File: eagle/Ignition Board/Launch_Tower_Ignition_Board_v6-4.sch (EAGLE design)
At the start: 43 parts, among them Q1 PMV45EN, U1 OPTOISOLATOR, U2 INVERT GATES, U3 SN65220DBV, U4 AND GATE

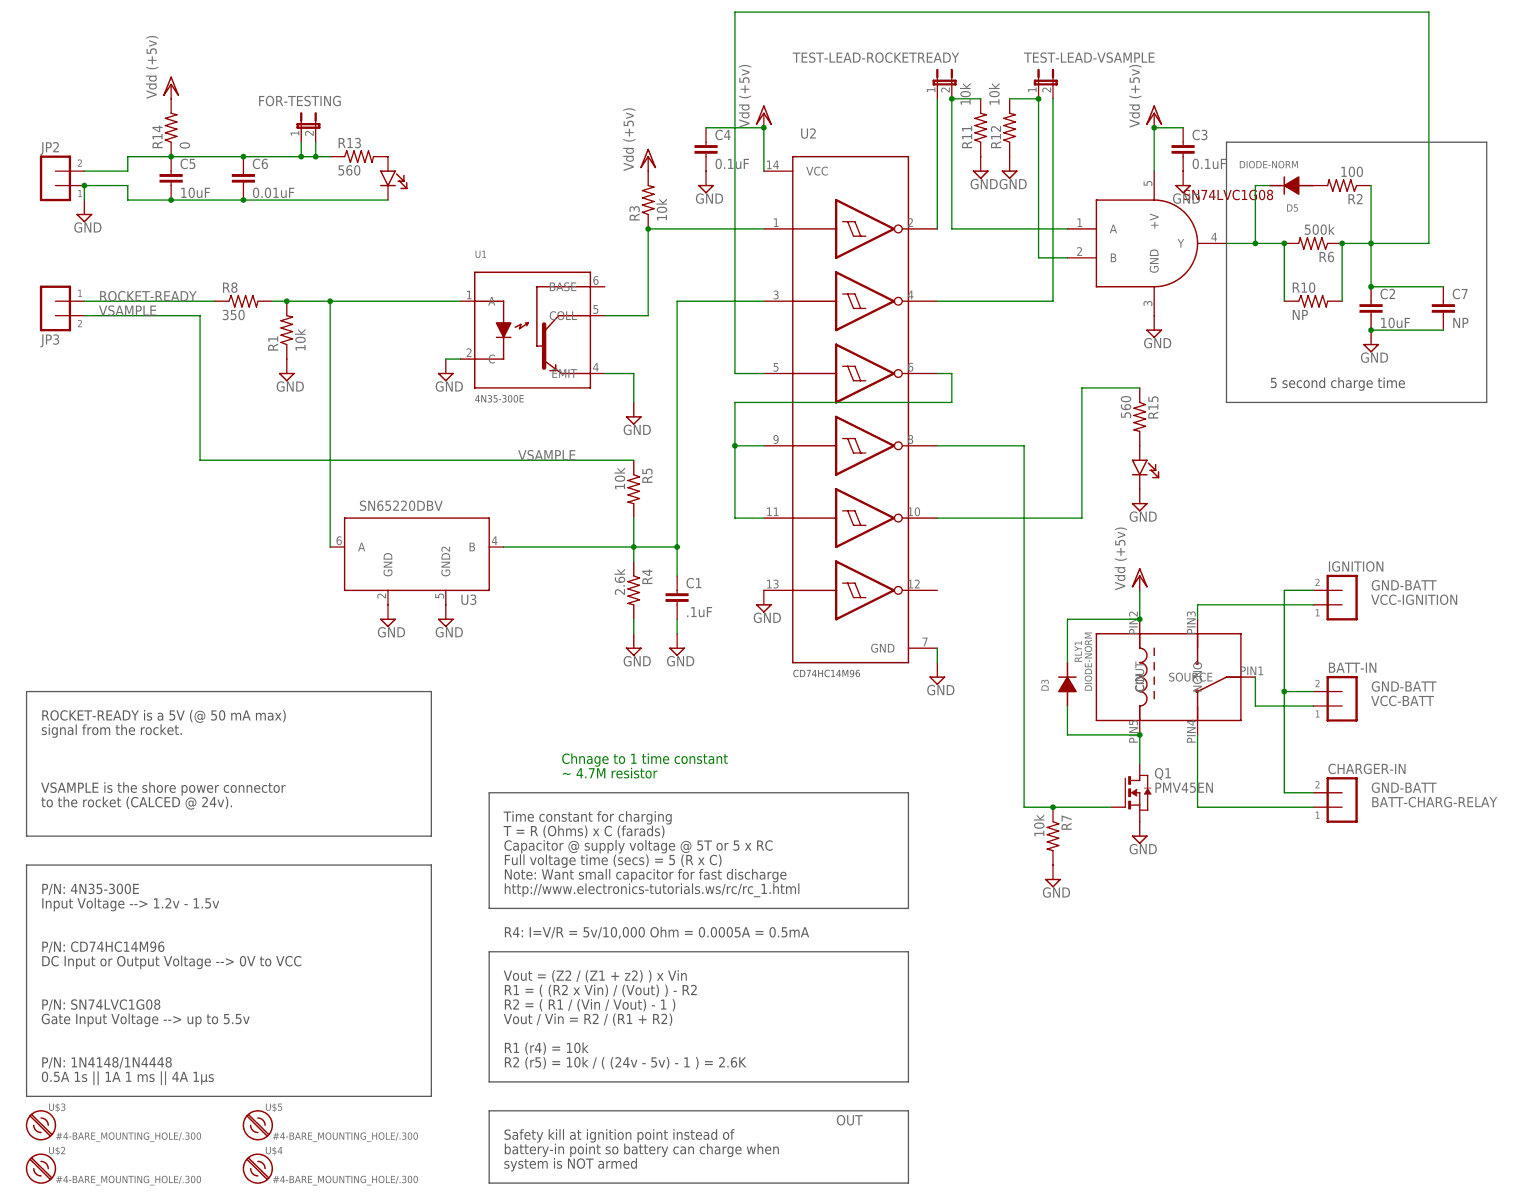
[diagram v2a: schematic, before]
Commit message: Updated Eagle File
Modified ignition board resistor R8
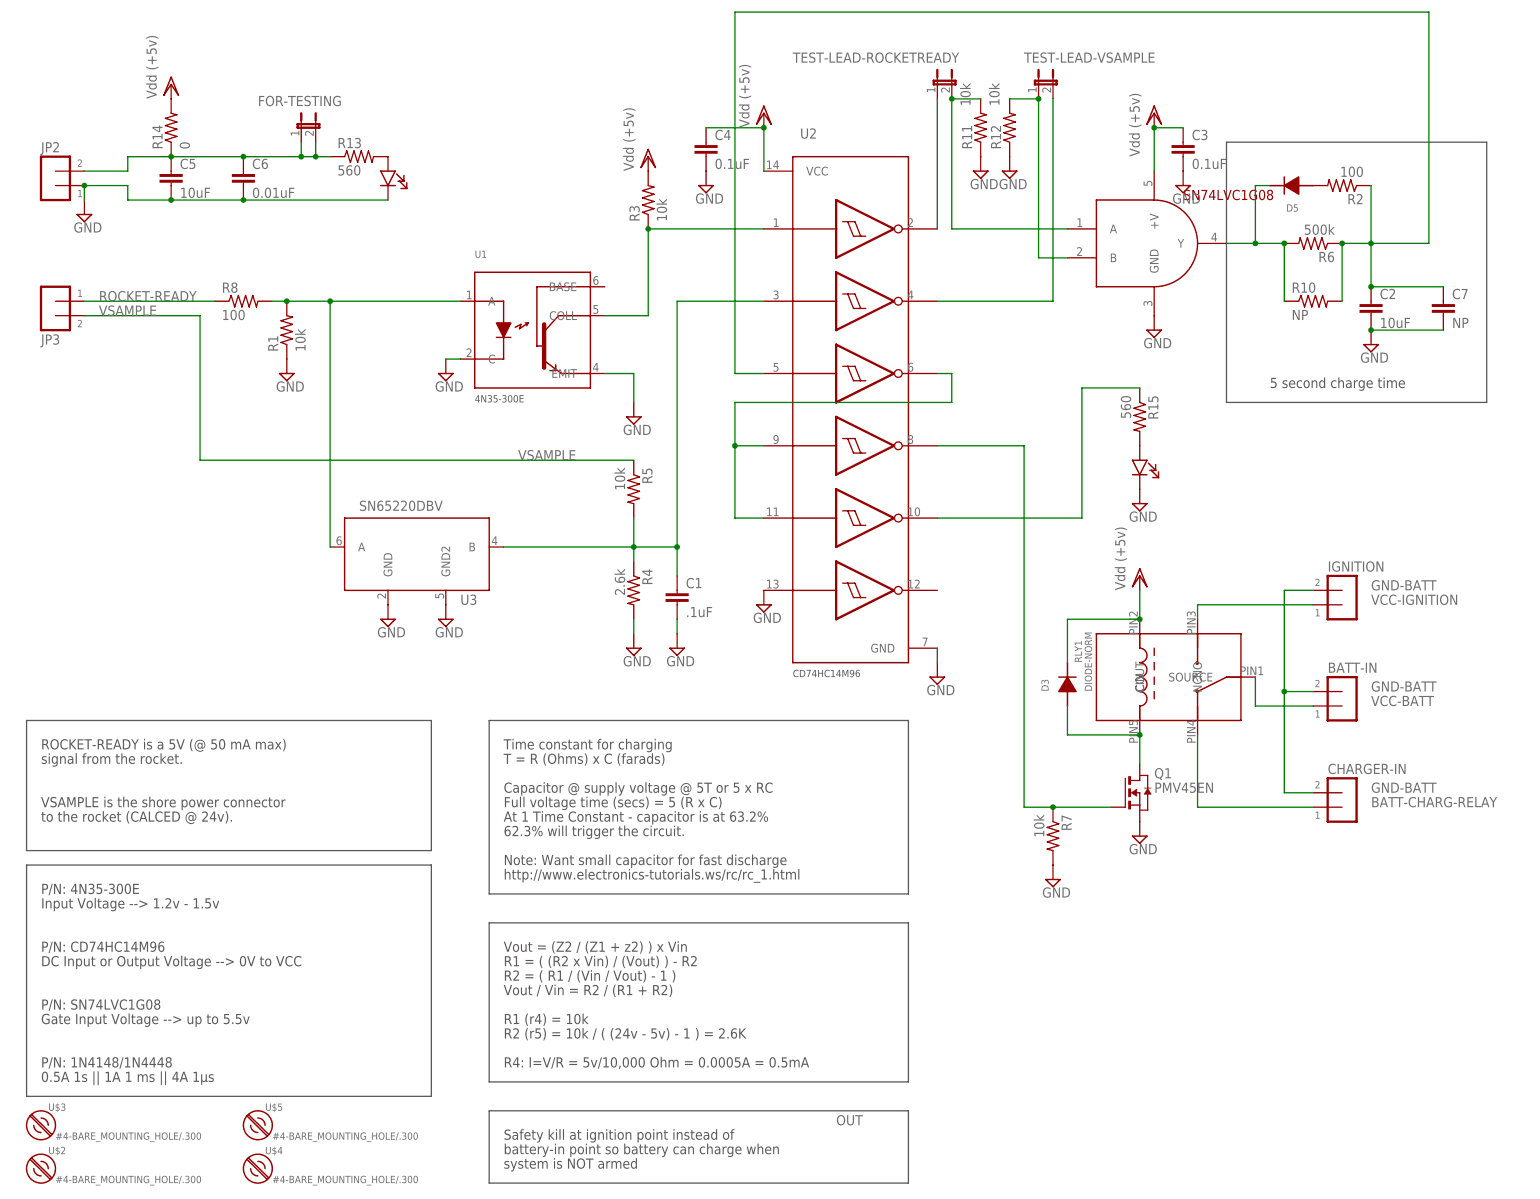
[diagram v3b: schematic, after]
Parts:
- R8: value 350 -> 100
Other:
- note added: "62.3% will trigger the circuit."
- note added: "At 1 Time Constant - capacitor is at 63.2%"
- note removed: "Chnage to 1 time constant"
- note removed: "~ 4.7M resistor"
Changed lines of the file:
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@@
 <?xml version="1.0" encoding="utf-8"?>
 <!DOCTYPE eagle SYSTEM "eagle.dtd">
-<eagle version="6.2">
+<eagle version="6.4">
 <drawing>
 <settings>
@@
 <part name="JP2" library="launch-tower" deviceset="SCREW-TERMINAL-5MM" device="" value=""/>
 <part name="JP3" library="launch-tower" deviceset="SCREW-TERMINAL-5MM" device="" value=""/>
-<part name="D5" library="launch-tower" deviceset="DIODE-NORM" device=""/>
+<part name="D5" library="launch-tower" deviceset="DIODE-NORM" device="" value=""/>
 <part name="D3" library="launch-tower" deviceset="DIODE-NORM" device=""/>
 <part name="VDD2" library="supply1" deviceset="VDD" device="" value="Vdd (+5v)"/>
@@
 <part name="TEST-LEAD-VSAMPLE" library="SparkFun" deviceset="JUMPER-2" device="PTH"/>
 <part name="LED-POWER-INDICATOR" library="launch-tower" deviceset="LED-550-XX04" device=""/>
-<part name="R8" library="rcl_custom" deviceset="R-US_" device="0805-B" value="350"/>
+<part name="R8" library="rcl_custom" deviceset="R-US_" device="0805-B" value="100"/>
 <part name="R1" library="rcl_custom" deviceset="R-US_" device="0805-B" value="10k"/>
 <part name="R3" library="rcl_custom" deviceset="R-US_" device="0805-B" value="10k"/>
@@
 <sheet>
 <plain>
-<text x="12.7" y="83.82" size="1.778" layer="97">ROCKET-READY is a 5V (@ 50 mA max)</text>
-<text x="12.7" y="81.28" size="1.778" layer="97">signal from the rocket.</text>
-<text x="12.7" y="71.12" size="1.778" layer="97">VSAMPLE is the shore power connector</text>
-<text x="12.7" y="68.58" size="1.778" layer="97">to the rocket (CALCED @ 24v).</text>
+<text x="12.7" y="78.74" size="1.778" layer="97">ROCKET-READY is a 5V (@ 50 mA max)</text>
+<text x="12.7" y="76.2" size="1.778" layer="97">signal from the rocket.</text>
+<text x="12.7" y="68.58" size="1.778" layer="97">VSAMPLE is the shore power connector</text>
+<text x="12.7" y="66.04" size="1.778" layer="97">to the rocket (CALCED @ 24v).</text>
 <text x="152.4" y="12.7" size="1.778" layer="104">OUT</text>
 <text x="152.4" y="12.7" size="1.778" layer="104">OUT</text>
 <text x="152.4" y="12.7" size="1.778" layer="95">OUT</text>
-<text x="93.98" y="45.72" size="1.778" layer="97">R4: I=V/R = 5v/10,000 Ohm = 0.0005A = 0.5mA</text>
-<text x="93.98" y="66.04" size="1.778" layer="97">Time constant for charging</text>
-<text x="93.98" y="63.5" size="1.778" layer="97">T = R (Ohms) x C (farads)</text>
-<text x="93.98" y="60.96" size="1.778" layer="97">Capacitor @ supply voltage @ 5T or 5 x RC</text>
-<text x="93.98" y="58.42" size="1.778" layer="97">Full voltage time (secs) = 5 (R x C)</text>
-<text x="93.98" y="55.88" size="1.778" layer="97">Note: Want small capacitor for fast discharge</text>
-<text x="93.98" y="38.1" size="1.778" layer="97">Vout = (Z2 / (Z1 + z2) ) x Vin</text>
-<text x="93.98" y="35.56" size="1.778" layer="97">R1 = ( (R2 x Vin) / (Vout) ) - R2</text>
-<text x="93.98" y="33.02" size="1.778" layer="97">R2 = ( R1 / (Vin / Vout) - 1 )</text>
-<text x="93.98" y="30.48" size="1.778" layer="97">Vout / Vin = R2 / (R1 + R2)</text>
+<text x="93.98" y="22.86" size="1.778" layer="97">R4: I=V/R = 5v/10,000 Ohm = 0.0005A = 0.5mA</text>
+<text x="93.98" y="78.74" size="1.778" layer="97">Time constant for charging</text>
+<text x="93.98" y="76.2" size="1.778" layer="97">T = R (Ohms) x C (farads)</text>
+<text x="93.98" y="71.12" size="1.778" layer="97">Capacitor @ supply voltage @ 5T or 5 x RC</text>
+<text x="93.98" y="68.58" size="1.778" layer="97">Full voltage time (secs) = 5 (R x C)</text>
+<text x="93.98" y="58.42" size="1.778" layer="97">Note: Want small capacitor for fast discharge</text>
+<text x="93.98" y="43.18" size="1.778" layer="97">Vout = (Z2 / (Z1 + z2) ) x Vin</text>
+<text x="93.98" y="40.64" size="1.778" layer="97">R1 = ( (R2 x Vin) / (Vout) ) - R2</text>
+<text x="93.98" y="38.1" size="1.778" layer="97">R2 = ( R1 / (Vin / Vout) - 1 )</text>
+<text x="93.98" y="35.56" size="1.778" layer="97">Vout / Vin = R2 / (R1 + R2)</text>
 <text x="12.7" y="20.32" size="1.778" layer="97">0.5A 1s || 1A 1 ms || 4A 1μs</text>
-<text x="93.98" y="25.4" size="1.778" layer="97">R1 (r4) = 10k</text>
+<text x="93.98" y="30.48" size="1.778" layer="97">R1 (r4) = 10k</text>
 <text x="12.7" y="30.48" size="1.778" layer="97">Gate Input Voltage --&gt; up to 5.5v</text>
 <text x="12.7" y="40.64" size="1.778" layer="97">DC Input or Output Voltage --&gt; 0V to VCC</text>
@@
 <text x="12.7" y="53.34" size="1.778" layer="97">P/N: 4N35-300E</text>
 <text x="12.7" y="50.8" size="1.778" layer="97">Input Voltage --&gt; 1.2v - 1.5v</text>
-<text x="93.98" y="22.86" size="1.778" layer="97">R2 (r5) = 10k / ( (24v - 5v) - 1 ) = 2.6K</text>
+<text x="93.98" y="27.94" size="1.778" layer="97">R2 (r5) = 10k / ( (24v - 5v) - 1 ) = 2.6K</text>
 <text x="12.7" y="22.86" size="1.778" layer="97">P/N: 1N4148/1N4448</text>
-<text x="93.98" y="53.34" size="1.778" layer="97">http://www.electronics-tutorials.ws/rc/rc_1.html</text>
+<text x="93.98" y="55.88" size="1.778" layer="97">http://www.electronics-tutorials.ws/rc/rc_1.html</text>
 <text x="228.6" y="142.24" size="1.778" layer="97">5 second charge time</text>
 <wire x1="220.98" y1="185.42" x2="220.98" y2="139.7" width="0.2032" layer="97"/>
@@
 <wire x1="266.7" y1="139.7" x2="266.7" y2="185.42" width="0.2032" layer="97"/>
 <wire x1="266.7" y1="185.42" x2="220.98" y2="185.42" width="0.2032" layer="97"/>
-<text x="104.14" y="76.2" size="1.778" layer="91">Chnage to 1 time constant</text>
-<text x="104.14" y="73.66" size="1.778" layer="91">~ 4.7M resistor</text>
 <text x="93.98" y="10.16" size="1.778" layer="97">Safety kill at ignition point instead of</text>
 <text x="93.98" y="7.62" size="1.778" layer="97">battery-in point so battery can charge when</text>
-<wire x1="91.44" y1="15.24" x2="91.44" y2="2.54" width="0.2032" layer="97"/>
-<wire x1="91.44" y1="2.54" x2="165.1" y2="2.54" width="0.2032" layer="97"/>
-<wire x1="165.1" y1="2.54" x2="165.1" y2="15.24" width="0.2032" layer="97"/>
-<wire x1="165.1" y1="15.24" x2="91.44" y2="15.24" width="0.2032" layer="97"/>
+<wire x1="91.44" y1="15.24" x2="91.44" y2="2.54" width="0.1524" layer="97"/>
+<wire x1="91.44" y1="2.54" x2="165.1" y2="2.54" width="0.1524" layer="97"/>
+<wire x1="165.1" y1="2.54" x2="165.1" y2="15.24" width="0.1524" layer="97"/>
+<wire x1="165.1" y1="15.24" x2="91.44" y2="15.24" width="0.1524" layer="97"/>
 <text x="93.98" y="5.08" size="1.778" layer="97">system is NOT armed</text>
-<wire x1="91.44" y1="20.32" x2="91.44" y2="43.18" width="0.1524" layer="97"/>
-<wire x1="91.44" y1="43.18" x2="165.1" y2="43.18" width="0.1524" layer="97"/>
+<wire x1="91.44" y1="20.32" x2="91.44" y2="48.26" width="0.1524" layer="97"/>
+<wire x1="91.44" y1="48.26" x2="165.1" y2="48.26" width="0.1524" layer="97"/>
 <wire x1="165.1" y1="20.32" x2="91.44" y2="20.32" width="0.1524" layer="97"/>
-<wire x1="165.1" y1="20.32" x2="165.1" y2="43.18" width="0.1524" layer="97"/>
-<wire x1="91.44" y1="50.8" x2="165.1" y2="50.8" width="0.1524" layer="97"/>
-<wire x1="165.1" y1="50.8" x2="165.1" y2="71.12" width="0.1524" layer="97"/>
-<wire x1="165.1" y1="71.12" x2="91.44" y2="71.12" width="0.1524" layer="97"/>
-<wire x1="91.44" y1="71.12" x2="91.44" y2="50.8" width="0.1524" layer="97"/>
-<wire x1="81.28" y1="63.5" x2="10.16" y2="63.5" width="0.1524" layer="97"/>
-<wire x1="10.16" y1="63.5" x2="10.16" y2="88.9" width="0.1524" layer="97"/>
-<wire x1="10.16" y1="88.9" x2="81.28" y2="88.9" width="0.1524" layer="97"/>
-<wire x1="81.28" y1="88.9" x2="81.28" y2="63.5" width="0.1524" layer="97"/>
+<wire x1="165.1" y1="20.32" x2="165.1" y2="48.26" width="0.1524" layer="97"/>
+<wire x1="91.44" y1="53.34" x2="165.1" y2="53.34" width="0.1524" layer="97"/>
+<wire x1="165.1" y1="53.34" x2="165.1" y2="83.82" width="0.1524" layer="97"/>
+<wire x1="165.1" y1="83.82" x2="91.44" y2="83.82" width="0.1524" layer="97"/>
+<wire x1="91.44" y1="83.82" x2="91.44" y2="53.34" width="0.1524" layer="97"/>
+<wire x1="81.28" y1="60.96" x2="10.16" y2="60.96" width="0.1524" layer="97"/>
+<wire x1="10.16" y1="60.96" x2="10.16" y2="83.82" width="0.1524" layer="97"/>
+<wire x1="10.16" y1="83.82" x2="81.28" y2="83.82" width="0.1524" layer="97"/>
+<wire x1="81.28" y1="83.82" x2="81.28" y2="60.96" width="0.1524" layer="97"/>
 <wire x1="10.16" y1="58.42" x2="81.28" y2="58.42" width="0.1524" layer="97"/>
 <wire x1="81.28" y1="58.42" x2="81.28" y2="17.78" width="0.1524" layer="97"/>
 <wire x1="81.28" y1="17.78" x2="10.16" y2="17.78" width="0.1524" layer="97"/>
 <wire x1="10.16" y1="17.78" x2="10.16" y2="58.42" width="0.1524" layer="97"/>
+<text x="93.98" y="66.04" size="1.778" layer="97">At 1 Time Constant - capacitor is at 63.2%</text>
+<text x="93.98" y="63.5" size="1.778" layer="97">62.3% will trigger the circuit.</text>
 </plain>
 <instances>
@@
 <instance part="U2" gate="A" x="154.94" y="144.78"/>
 <instance part="U1" gate="G$1" x="99.06" y="152.4"/>
-<instance part="U4" gate="G$1" x="200.66" y="162.56"/>
+<instance part="U4" gate="G$1" x="200.66" y="162.56" smashed="yes"/>
 <instance part="SUPPLY3" gate="GND" x="55.88" y="144.78"/>
 <instance part="SUPPLY4" gate="GND" x="83.82" y="144.78"/>
@@
 <instance part="SUPPLY10" gate="GND" x="170.18" y="91.44"/>
 <instance part="VDD3" gate="G$1" x="139.7" y="190.5"/>
-<instance part="VDD4" gate="G$1" x="208.28" y="190.5"/>
+<instance part="VDD4" gate="G$1" x="208.28" y="190.5" smashed="yes">
+<attribute name="VALUE" x="205.74" y="182.88" size="1.778" layer="96" rot="R90"/>
+</instance>
 <instance part="SUPPLY11" gate="GND" x="208.28" y="152.4"/>
 <instance part="VDD5" gate="G$1" x="205.74" y="109.22"/>
